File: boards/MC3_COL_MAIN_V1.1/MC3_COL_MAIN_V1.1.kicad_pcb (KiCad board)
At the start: 4 copper layers, 66 x 66 mm, 137 parts, among them J1 SUPPLY_IN, J10 MOTOR, J11 MOTOR, J12 CAN, J2 SWD, J3 ENC_leaf1, J4 ENC_leaf2, J5 ENC_leaf3, J6 ENC_leaf4, J7 MOTOR, J8 MOTOR, J9 MOTOR, Q1 AO4407C, SW1 SKRKAEE020, U1 AMS1117-3.3, U10 GP1S094HCZ0F, U11 GP1S094HCZ0F, U2 STM32U595RJT6, U3 DRV8214RTER, U4 DRV8214RTER, U5 DRV8214RTER, U6 DRV8214RTER, U7 DRV8214RTER, U8 TJA1051T/3, U9 AEDR-8300-1Q0, Y1 8MHz

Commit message: V1.1 Power sheet: buck section redrawn as a wired left-to-right chain (netlist unchanged, ERC 0 errors)
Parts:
- removed J11: MOTOR, MC3_COL_MAIN:SolderPads_2x_2.2x1.4mm_P2.6mm
- added C48: 10uF 50V, MC3_COL_MAIN:C_1210_3225Metric, F.Cu at (130.5, 97.5)
- added C49: 10uF 50V, MC3_COL_MAIN:C_1210_3225Metric, F.Cu at (127.2, 97.5)
- added C50: 100nF 50V, MC3_COL_MAIN:C_0603_1608Metric, F.Cu at (153.6, 100.1)
- added C51: 1nF, MC3_COL_MAIN:C_0402_1005Metric, F.Cu at (148.1, 91.3)
- added C52: 100nF, MC3_COL_MAIN:C_0402_1005Metric, F.Cu at (148.1, 93.3)
- added C53: 1uF, MC3_COL_MAIN:C_0603_1608Metric, F.Cu at (153.6, 102.6)
- added C54: 100nF, MC3_COL_MAIN:C_0402_1005Metric, F.Cu at (148.1, 95.2)
- added C55: 4.7pF, MC3_COL_MAIN:C_0402_1005Metric, F.Cu at (148.1, 97.2)
- added C56: 22uF 25V, MC3_COL_MAIN:C_0805_2012Metric, F.Cu at (149.3, 100.3)
- added C57: 22uF 25V, MC3_COL_MAIN:C_0805_2012Metric, F.Cu at (148.7, 103.3)
- added D7: BZT52C12, MC3_COL_MAIN:D_SOD-123, B.Cu at (122.2, 105.0)
- added J13: HARNESS_FFC_6P, MC3_COL_MAIN:TE_84952-6_1x06-1MP_P1.0mm_Horizontal, B.Cu at (124.3, 94.6)
- added L1: 2.2uH XAL5030-222, MC3_COL_MAIN:L_Coilcraft_XAL5030-XXX, F.Cu at (128.2, 108.5)
- added R41: 13.3k, MC3_COL_MAIN:R_0402_1005Metric, F.Cu at (142.2, 91.3)
- added R42: 100k, MC3_COL_MAIN:R_0402_1005Metric, B.Cu at (131.4, 104.9)
- added R43: 8.66k, MC3_COL_MAIN:R_0402_1005Metric, B.Cu at (130.4, 104.8)
- added R44: 0R, MC3_COL_MAIN:R_0402_1005Metric, F.Cu at (142.2, 97.3)
- added R45: 100k, MC3_COL_MAIN:R_0402_1005Metric, F.Cu at (142.2, 99.3)
- added R46: 24.9k, MC3_COL_MAIN:R_0402_1005Metric, F.Cu at (142.2, 101.2)
- added R47: 1k, MC3_COL_MAIN:R_0402_1005Metric, F.Cu at (142.2, 103.2)
- added U12: LM61460AANRJRR, MC3_COL_MAIN:VQFN-HR14_RJR_TEX, F.Cu at (128.4, 102.4)
- D1: value SMAJ5.0A -> SMAJ28A; moved to B.Cu
- F1: value 2A hold/3.5A trip -> 0.75A hold 33V; moved to B.Cu
- Q1: value AO4407C -> AO4421; moved to B.Cu
- R5: moved to B.Cu
- moved TP7 30.8 mm to (108.8, 129.1)
- moved J12 26.1 mm to (115.2, 124.9)
- moved J1 13.0 mm to (116.5, 103.0), turned to -90 degrees
- moved D1 5.30 mm to (128.2, 101.8), turned to 90 degrees
- moved TP2 3.46 mm to (128.4, 107.4)
- moved R5 3.05 mm to (125.3, 104.5), turned to -90 degrees
- moved Q1 2.34 mm to (122.5, 101.1), turned to 180 degrees
- moved C1 1.58 mm to (116.5, 97.9)
- moved C3 1.58 mm to (116.5, 100.1)
- moved C4 1.58 mm to (116.5, 102.4)
- moved H5 1.33 mm to (100.2, 72.5)
- moved F1 1.10 mm to (131.2, 101.2)
- moved H4 0.88 mm to (125.9, 85.0)
- moved C45 0.23 mm to (114.6, 97.8)
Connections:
- net /CAN/CANL renamed CANL
- net /Power/VIN_PAD renamed VIN_PAD
- D4 pad 1: /CAN/CANH -> CANH
- J12 pad 1: /CAN/CANH -> CANH
- JP1 pad 1: /CAN/CANH -> CANH
- Q1 pad 1: VM -> /Power/VIN_SW
- Q1 pad 2: VM -> /Power/VIN_SW
- Q1 pad 3: VM -> /Power/VIN_SW
- U2 pad 56: unconnected-(U2-PB4-Pad56) -> BUCK_SYNC
- U7 pad 6: /yaw/OUT1 -> YAW_OUT1
- U7 pad 8: /yaw/OUT2 -> YAW_OUT2
- U8 pad 7: /CAN/CANH -> CANH
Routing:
- net YAW_OUT1: track 0.00 -> 44.6 mm, vias 0 -> 1
- net YAW_OUT2: track 0.00 -> 44.1 mm, vias 0 -> 1
- net /MCU/YAW_HOME: track 25.0 -> 63.4 mm
- net RC_OUT_leaf1: track 48.0 -> 28.7 mm, vias 4 -> 3
- net VIN_PROT: track 15.8 -> 0.00 mm, vias 1 -> 0
- net CANL: track 49.7 -> 35.9 mm
- net BUCK_SYNC: track 0.00 -> 12.2 mm
- net /CAN/CANH: track 59.8 -> 48.2 mm
- net VIN_PAD: track 6.35 -> 0.00 mm, vias 2 -> 0
- net VM: track 200.8 -> 194.6 mm, vias 3 -> 2
- net IPROPI_leaf1: track 88.2 -> 82.8 mm
- net /yaw/OUT2: track 4.33 -> 0.00 mm
- net /yaw/OUT1: track 2.75 -> 0.00 mm
- net VSENS: track 49.8 -> 48.4 mm
- net /Power/Q1_G: track 1.33 -> 0.00 mm
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- removed copper zone on B.Cu, net GND

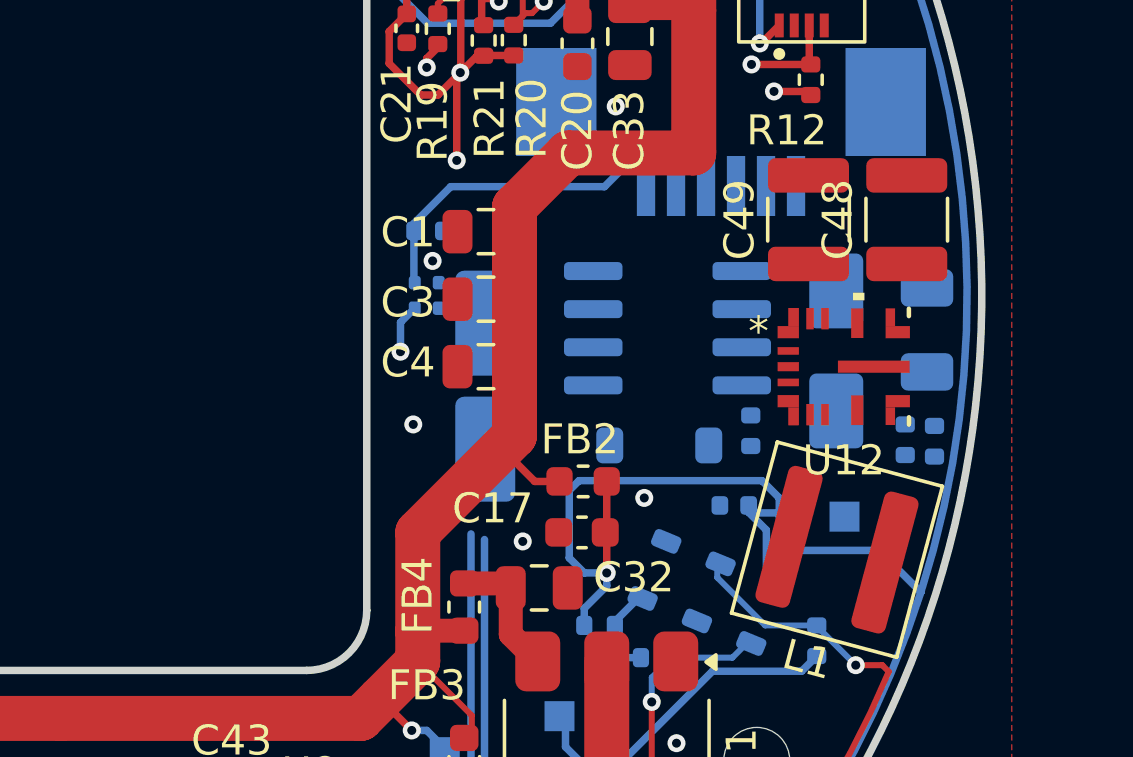
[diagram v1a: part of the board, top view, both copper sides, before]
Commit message: V1.1 Power: named labels restored on BUCK_EN/RT/BOOT/VCC nodes
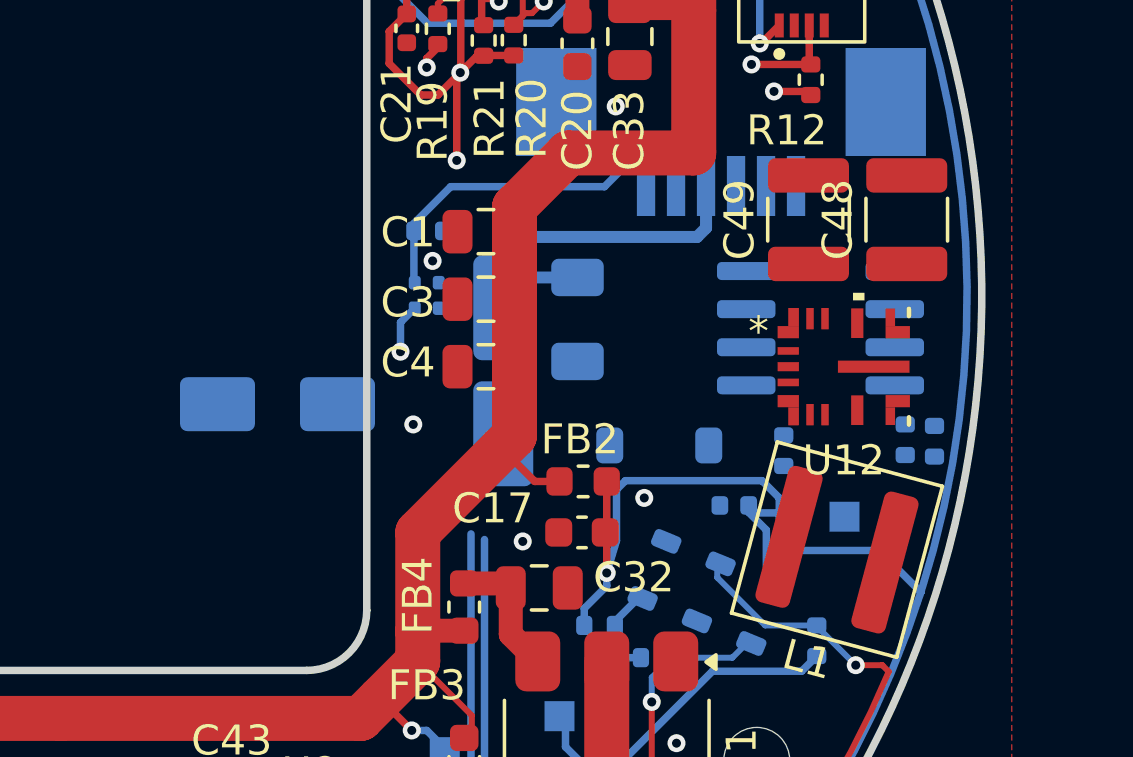
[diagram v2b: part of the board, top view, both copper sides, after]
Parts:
- moved D1 18.7 mm to (109.5, 103.6), turned to 180 degrees
- moved F1 11.7 mm to (119.5, 100.8)
- moved Q1 5.10 mm to (127.6, 101.1)
- moved R5 1.29 mm to (126.4, 105.2)
- moved J1 0.79 mm to (117.0, 102.5)
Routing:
- net VIN_PAD: track 0.00 -> 13.2 mm
- net VSENS: track 48.4 -> 45.9 mm
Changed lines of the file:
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@@
 		(tags "te fpc 84952")
 		(property "Reference" "J13"
-			(at 0 4 0)
+			(at 0 -0.477378 0)
 			(layer "B.SilkS")
 			(effects
@@
 	(footprint "MC3_COL_MAIN:SolderPads_2x_3.5x2.0mm_P4.2mm"
 		(layer "B.Cu")
-		(at 116.45 103.025 -90)
+		(at 117.05 102.5125 -90)
 		(descr "Machine supply termination: two bare solder pads 3.5 x 2.0 mm on 4.2 mm pitch, top copper, hand-soldered 20-22 AWG lead, whole-board current. Vault: Main-Board-01 Connectors, Machine Interface. No part, no paste.")
 		(tags "solder pad supply termination bare copper")
@@
 	(footprint "MC3_COL_MAIN:R_0402_1005Metric"
 		(layer "B.Cu")
-		(at 125.3 104.51 -90)
+		(at 126.4 105.175 -90)
 		(descr "Resistor SMD 0402 (1005 Metric), square (rectangular) end terminal, IPC-7351 nominal, (Body size source: IPC-SM-782 page 72, https://www.pcb-3d.com/wordpress/wp-content/uploads/ipc-sm-782a_amendment_1_and_2.pdf)")
 		(tags "resistor")
@@
 	(footprint "MC3_COL_MAIN:SOIC-8_3.9x4.9mm_P1.27mm"
 		(layer "B.Cu")
-		(at 122.525 101.0925 180)
+		(at 127.625 101.0925 180)
 		(descr "SOIC, 8 Pin (JEDEC MS-012AA, https://www.analog.com/media/en/package-pcb-resources/package/pkg_pdf/soic_narrow-r/r_8.pdf)")
 		(tags "SOIC SO")
 		(property "Reference" "Q1"
-			(at 0.875 3.485 0)
+			(at -0.05 0.0925 0)
 			(layer "B.SilkS")
 			(effects
@@
 	(footprint "MC3_COL_MAIN:D_SMA"
 		(layer "B.Cu")
-		(at 128.15 101.85 90)
+		(at 109.525 103.625 180)
 		(descr "Diode SMA (DO-214AC)")
 		(tags "Diode SMA (DO-214AC)")
 		(property "Reference" "D1"
-			(at -4.8 0.3 90)
+			(at -4.8 0.3 0)
 			(layer "B.SilkS")
 			(effects
@@
 		)
 		(property "Value" "SMAJ28A"
-			(at 0 -2.6 90)
+			(at 0 -2.6 0)
 			(layer "B.Fab")
 			(effects
@@
 		)
 		(property "Datasheet" ""
-			(at 0 0 270)
+			(at 0 0 0)
 			(unlocked yes)
 			(layer "B.Fab")
@@
 		)
 		(property "Description" ""
-			(at 0 0 270)
+			(at 0 0 0)
 			(unlocked yes)
 			(layer "B.Fab")
@@
 		)
 		(property "Note" "TVS SMAJ5.0A (unidirectional, 5 V standoff) VIN_PROT to GND, after the fuse. Cathode to VIN_PROT. LCSC TBD. Review item 5 / vault no-input-protection open item"
-			(at 0 0 270)
+			(at 0 0 0)
 			(unlocked yes)
 			(layer "B.Fab")
@@
 		)
 		(property "LCSC" "C78401"
-			(at 0 0 270)
+			(at 0 0 0)
 			(unlocked yes)
 			(layer "B.Fab")
@@
 		)
 		(property "MPN" "SMAJ5.0A/TR13"
-			(at 0 0 270)
+			(at 0 0 0)
 			(unlocked yes)
 			(layer "B.Fab")
@@
 		(duplicate_pad_numbers_are_jumpers no)
 		(fp_line
-			(start -3.51 -1.65)
-			(end 2 -1.65)
+			(start -3.51 1.65)
+			(end 2 1.65)
 			(stroke
 				(width 0.12)
@@
 		)
 		(fp_line
-			(start -3.51 1.65)
-			(end 2 1.65)
+			(start -3.51 -1.65)
+			(end 2 -1.65)
 			(stroke
 				(width 0.12)
@@
 		)
 		(fp_line
-			(start 3.5 -1.75)
-			(end -3.5 -1.75)
+			(start 3.5 1.75)
+			(end 3.5 -1.75)
 			(stroke
 				(width 0.05)
@@
 		)
 		(fp_line
-			(start -3.5 -1.75)
-			(end -3.5 1.75)
+			(start 3.5 -1.75)
+			(end -3.5 -1.75)
 			(stroke
 				(width 0.05)
@@
 		)
 		(fp_line
-			(start 3.5 1.75)
-			(end 3.5 -1.75)
+			(start -3.5 1.75)
+			(end 3.5 1.75)
 			(stroke
 				(width 0.05)
@@
 		)
 		(fp_line
-			(start -3.5 1.75)
-			(end 3.5 1.75)
+			(start -3.5 -1.75)
+			(end -3.5 1.75)
 			(stroke
 				(width 0.05)
@@
 		)
 		(fp_line
-			(start 2.3 -1.5)
-			(end -2.3 -1.5)
+			(start 2.3 1.5)
+			(end 2.3 -1.5)
 			(stroke
 				(width 0.1)
@@
 		)
 		(fp_line
-			(start -2.3 -1.5)
+			(start 2.3 1.5)
 			(end -2.3 1.5)
 			(stroke
@@
 		)
 		(fp_line
-			(start 0.50118 -0.75032)
-			(end 0.50118 0.79908)
+			(start 2.3 -1.5)
+			(end -2.3 -1.5)
 			(stroke
 				(width 0.1)
@@
 		)
 		(fp_line
-			(start -0.64944 -0.00102)
-			(end 0.50118 -0.75032)
+			(start 0.50118 -0.75032)
+			(end 0.50118 0.79908)
 			(stroke
 				(width 0.1)
@@
 		)
 		(fp_line
-			(start -0.64944 -0.00102)
-			(end -1.55114 -0.00102)
+			(start -0.64944 0.79908)
+			(end -0.64944 -0.80112)
 			(stroke
 				(width 0.1)
@@
 		)
 		(fp_line
-			(start -0.64944 0.79908)
-			(end -0.64944 -0.80112)
+			(start -0.64944 -0.00102)
+			(end 0.50118 -0.75032)
 			(stroke
 				(width 0.1)
@@
 		)
 		(fp_line
-			(start 2.3 1.5)
-			(end 2.3 -1.5)
+			(start -0.64944 -0.00102)
+			(end -1.55114 -0.00102)
 			(stroke
 				(width 0.1)
@@
 		)
 		(fp_line
-			(start 2.3 1.5)
+			(start -2.3 -1.5)
 			(end -2.3 1.5)
 			(stroke
@@
 		)
 		(fp_text user "${REFERENCE}"
-			(at 0 2.5 90)
+			(at 0 2.5 0)
 			(layer "B.Fab")
 			(effects
@@
 		)
 		(pad "1" smd roundrect
-			(at -2 0 90)
+			(at -2 0 180)
 			(size 2.5 1.8)
 			(layers "B.Cu" "B.Mask" "B.Paste")
@@
 		)
 		(pad "2" smd roundrect
-			(at 2 0 90)
+			(at 2 0 180)
 			(size 2.5 1.8)
 			(layers "B.Cu" "B.Mask" "B.Paste")
@@
 	(footprint "MC3_COL_MAIN:Fuse_1206_3216Metric"
 		(layer "B.Cu")
-		(at 131.175 101.15 -90)
+		(at 119.525 100.8 -90)
 		(descr "Fuse SMD 1206 (3216 Metric), square (rectangular) end terminal, IPC-7351 nominal, (Body size source: http://www.tortai-tech.com/upload/download/2011102023233369053.pdf)")
 		(tags "fuse")
@@
 	)
 	(segment
-		(start 126.25 106.75)
-		(end 126.25 107.25)
-		(width 0.25)
-		(layer "B.Cu")
-		(net "VSENS")
-	)
-	(segment
 		(start 125.6 91.6)
 		(end 125.6 89.5)
@@
 	)
 	(segment
-		(start 119.25 108.75)
-		(end 119.25 106.5)
-		(width 0.25)
-		(layer "B.Cu")
-		(net "VSENS")
-	)
-	(segment
 		(start 109.5 71.3)
 		(end 110.528216 70.271784)
@@
 	)
 	(segment
-		(start 119.25 106.5)
-		(end 119.575 106.175)
-		(width 0.25)
-		(layer "B.Cu")
-		(net "VSENS")
-	)
-	(segment
-		(start 120.5 109.25)
-		(end 119.75 109.25)
+		(start 126.25 106.75)
+		(end 126.25 107.25)
 		(width 0.25)
 		(layer "B.Cu")
@@
 	)
 	(segment
-		(start 119.575 106.175)
-		(end 125.675 106.175)
+		(start 125.675 106.175)
+		(end 126.25 106.75)
+		(width 0.25)
+		(layer "B.Cu")
+		(net "VSENS")
+	)
+	(segment
+		(start 120.5 109.25)
+		(end 120.825 108.175)
 		(width 0.25)
 		(layer "B.Cu")
@@
 	)
 	(segment
-		(start 125.675 106.175)
-		(end 126.25 106.75)
-		(width 0.25)
-		(layer "B.Cu")
-		(net "VSENS")
-	)
-	(segment
-		(start 119.75 109.25)
-		(end 119.25 108.75)
+		(start 121.125 106.175)
+		(end 125.675 106.175)
 		(width 0.25)
 		(layer "B.Cu")
@@
 	)
 	(segment
+		(start 120.825 108.175)
+		(end 120.825 106.475)
+		(width 0.25)
+		(layer "B.Cu")
+		(net "VSENS")
+	)
+	(segment
 		(start 125.23 107)
 		(end 125.23 107.23)
@@
 	)
 	(segment
+		(start 120.825 106.475)
+		(end 121.125 106.175)
+		(width 0.25)
+		(layer "B.Cu")
+		(net "VSENS")
+	)
+	(segment
 		(start 93.275 129.8)
 		(end 93.275 130.025)
@@
 	)
 	(segment
+		(start 117.05 98.662501)
+		(end 117.05 100.4125)
+		(width 0.4)
+		(layer "B.Cu")
+		(net "VIN_PAD")
+	)
+	(segment
+		(start 119.525 99.4)
+		(end 118.0625 99.4)
+		(width 0.4)
+		(layer "B.Cu")
+		(net "VIN_PAD")
+	)
+	(segment
+		(start 118.0625 99.4)
+		(end 117.05 100.4125)
+		(width 0.4)
+		(layer "B.Cu")
+		(net "VIN_PAD")
+	)
+	(segment
+		(start 123.81 96.352378)
+		(end 123.81 97.752378)
+		(width 0.4)
+		(layer "B.Cu")
+		(net "VIN_PAD")
+	)
+	(segment
+		(start 117.662501 98.05)
+		(end 117.05 98.662501)
+		(width 0.4)
+		(layer "B.Cu")
+		(net "VIN_PAD")
+	)
+	(segment
+		(start 123.512378 98.05)
+		(end 117.662501 98.05)
+		(width 0.4)
+		(layer "B.Cu")
+		(net "VIN_PAD")
+	)
+	(segment
+		(start 123.81 97.752378)
+		(end 123.512378 98.05)
+		(width 0.4)
+		(layer "B.Cu")
+		(net "VIN_PAD")
+	)
+	(segment

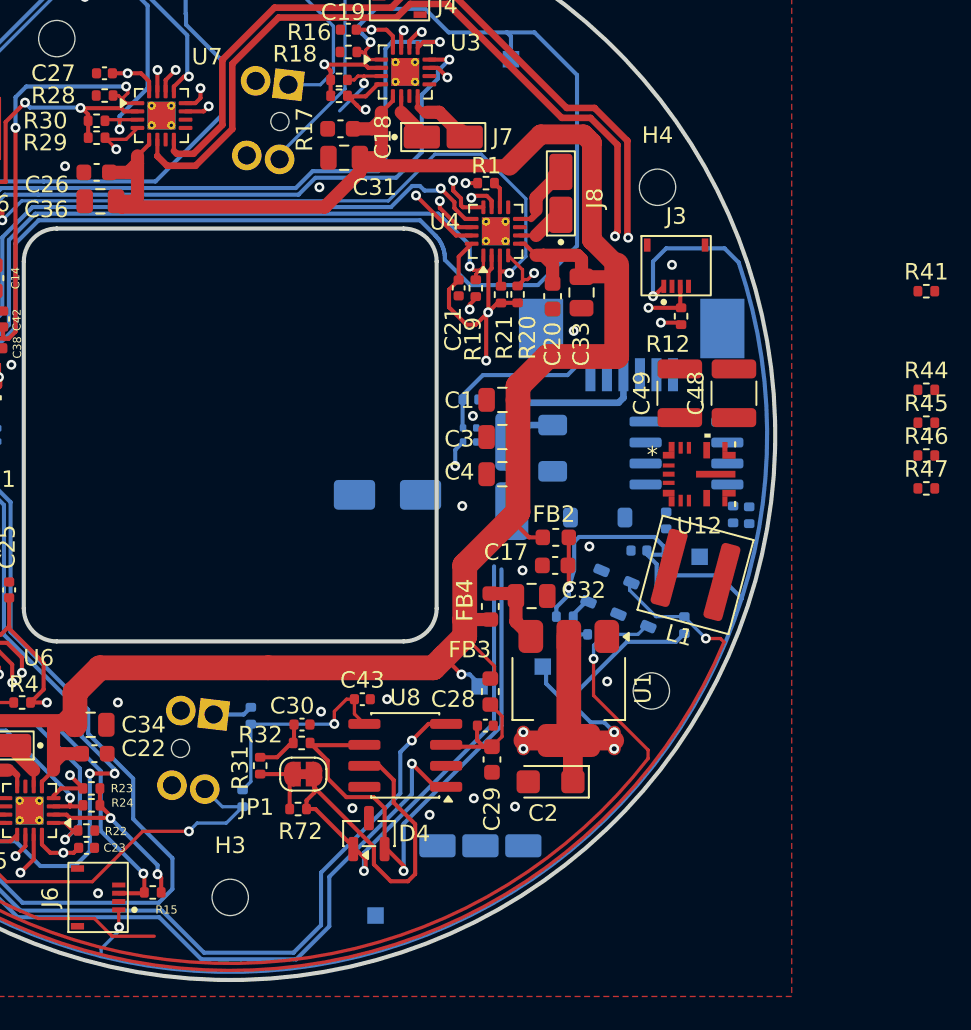
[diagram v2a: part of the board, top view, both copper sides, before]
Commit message: V1.1: J13 pin order mirrored (CANL CANH GND VIN OUT1 OUT2) for routing
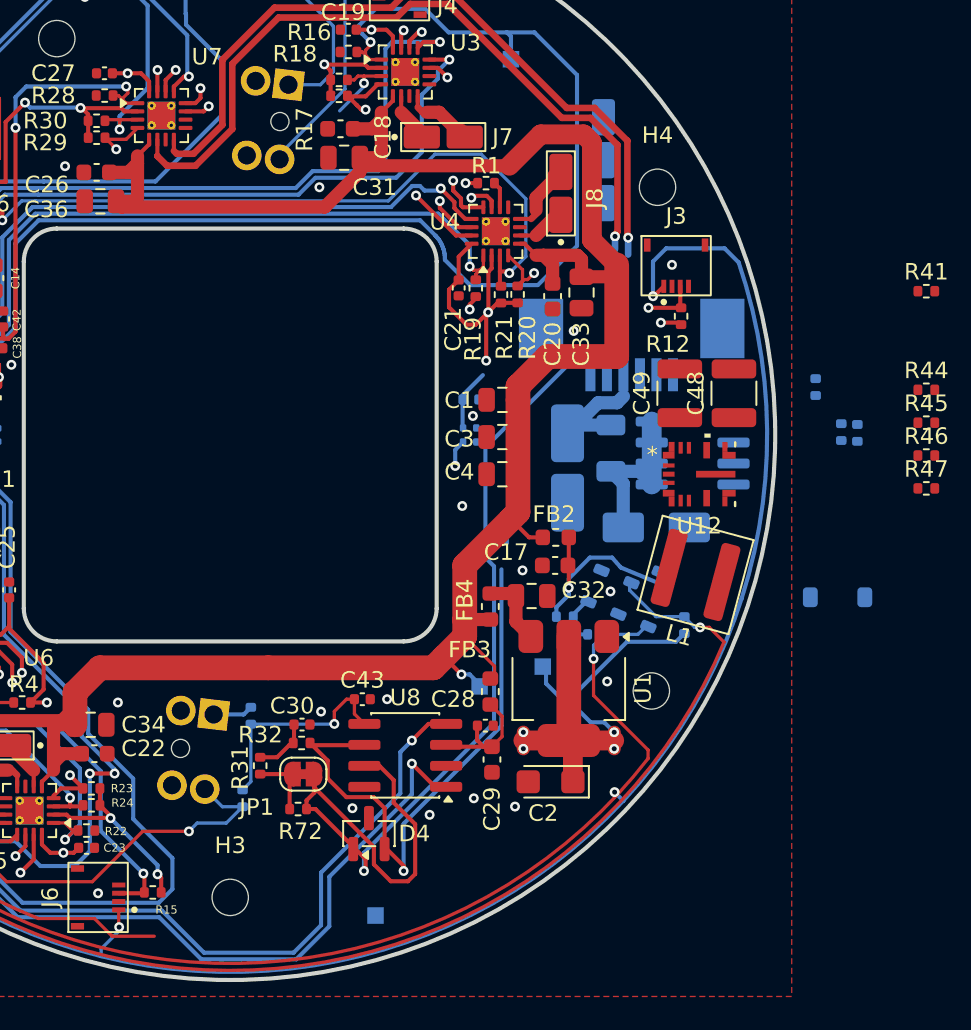
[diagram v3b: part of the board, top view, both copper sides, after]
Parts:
- moved J12 42.2 mm to (122.6, 83.4), turned to -90 degrees
- moved D1 16.4 mm to (125.8, 105.6), turned to 0 degrees
- moved D7 15.3 mm to (136.8, 109.8)
- moved R5 12.1 mm to (135.4, 97.1)
- moved TP2 12.1 mm to (116.4, 106.1)
- moved R43 8.23 mm to (137.0, 99.8)
- moved R42 8.23 mm to (138.0, 99.9)
- moved F1 3.52 mm to (123.0, 100.8)
- moved J1 3.41 mm to (120.4, 102.0)
- moved C37 2.09 mm to (126.3, 108.4), turned to 157.5 degrees
- moved Q1 0.38 mm to (128.0, 101.1)
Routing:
- net CANH: track 0.00 -> 38.1 mm
- net /CAN/CANH: track 48.2 -> 26.5 mm
- net VIN_PROT: track 0.00 -> 10.2 mm
- net VM: track 194.6 -> 187.8 mm
- net VIN_PAD: track 13.2 -> 8.45 mm
- net VSENS: track 45.9 -> 50.5 mm, vias 5 -> 6
- net YAW_OUT2: track 44.1 -> 45.2 mm
- net YAW_OUT1: track 44.6 -> 45.4 mm
